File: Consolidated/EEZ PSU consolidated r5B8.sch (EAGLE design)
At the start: 517 parts, among them IC1 LTC3864, IC10 REF5025, IC11 DAC8552, IC12 ADG465SOT-23, IC13 TS5A9411DCKT, IC14 ADS1120, IC15 LP339D, IC16 LM25575, IC17 MC7812, IC18 TPD4E002DRLR, IC19 TPD2E001DZDR, IC2 MC79L05, IC20 ADUM3160BRWZ, IC21 TLC5925IDBQR, IC22 Si8641EC-B-IS1, IC23 SI8651EC-B-IS1, IC24 SI8651EC-B-IS1, IC25 LD1117ADT33TR, IC26 Si8641EC-B-IS1, IC27 PCA21125, IC28 AT25256B, IC29 W5500, IC3 MC78L05, IC30 BC857BS, IC31 TLC555, IC32 SN74LVC2G08DCTR, IC33 TPS3705-33D, IC34 SN74LV1T34DBVR, IC35 SN74LVC2G02DCTR, IC4 LM5574, IC5 LP2951SO8, IC6 TL072D, IC7 TL072D, IC8 OP27GSZ, IC9 MCP23S08-E/SO, J1 BS-244DSM-R, J2 BS-244DSM-G, J3 BS-244DSM-B, J4 BS-244DSM-R, J5 BS-244DSM-B, Q1 SUD19P06-60, Q10 MMBT5401, Q11 MMBT5401, Q12 MMBT5551, Q13 MMBT5551, Q14 BSS84P, Q15 2N7002, Q16 MMBT5551, Q17 MMBT5401, Q18 MMBT5551, Q19 MMBT5551, Q2 MMBT5401, Q20 BTA26-600, Q21 BTA26-600, Q22 IRLL014N, Q23 IRLML2246TRPBF, Q24 IRLML2246TRPBF, Q25 IRLML2246TRPBF, Q26 IRLML2246TRPBF, Q27 2N7002, Q28 IRLML2246TRPBF, Q29 2N7002, Q3 2N7002, Q30 2N7002, Q4 IRFP250N, Q5 BC857C, Q6 BC846C, Q7 BCP56-16.115, Q8 IRFR5410, Q9 BCP56-16.115, SW1 A101SYCQ04, SW2 1301.9316, X1 282836-3, X10 826629-5, X11 2411-01, X12 MC000006, X13 TSW-113-07-F-D, X14 MC000005, X15 TSW-113-07-F-D, X16 09185067324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

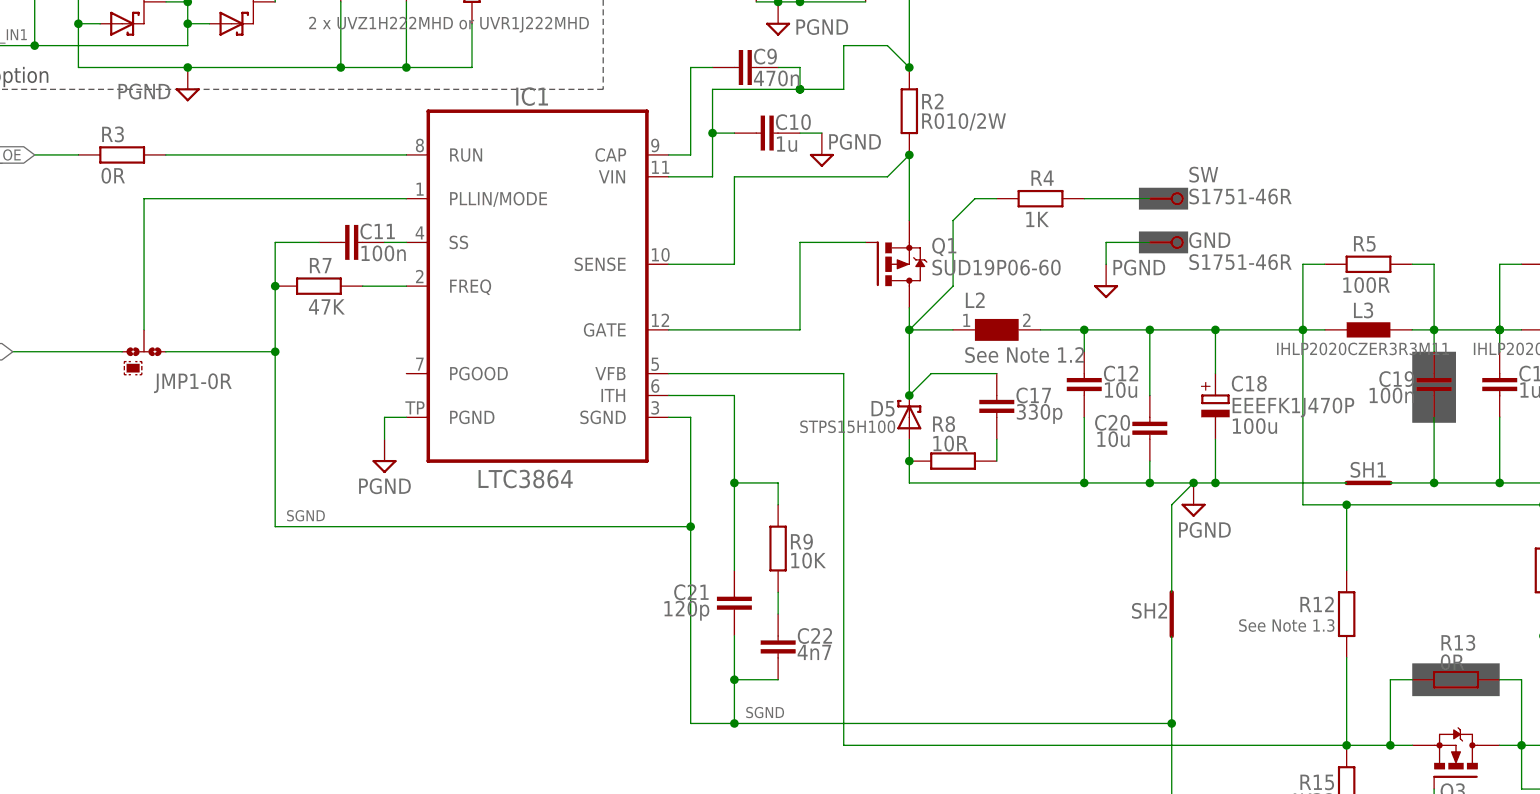
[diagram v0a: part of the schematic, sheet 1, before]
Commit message: Consolidated PCB, jumpers renumbering
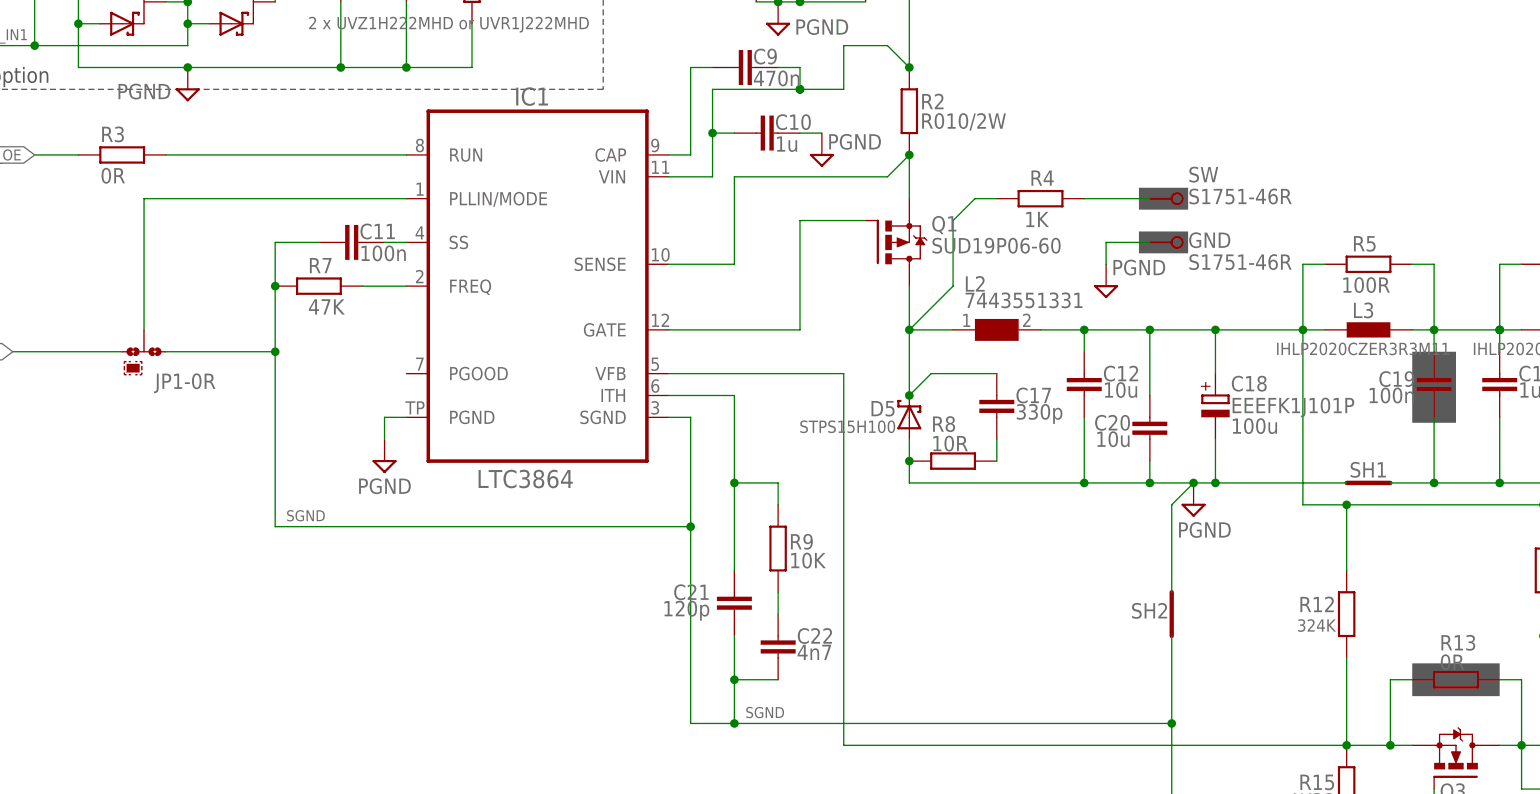
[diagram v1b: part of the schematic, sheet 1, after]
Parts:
- removed JMP1, JMP2: 0R-JUMPA, jump-0r-smd:0R-JUMPA
- added JP6, JP7: 0R-JUMPA, jump-0r-smd:0R-JUMPA
- C18: value EEEFK1J470P -> EEEFK1J101P
- D28: device diode:DIODE-DO214AC -> EEZ_Lib1:SCHOTTKYSOD123
- FB6, FB7: value 2506033007Y3 -> 60R@100MHz
- JP1: value 826926-2 -> 0R-JUMPA; device jumper:JP1E -> jump-0r-smd:0R-JUMPA
- JP3: value 0R-JUMPA -> 826926-2; device jump-0r-smd:0R-JUMPA -> jumper:JP1E
- L2: value See Note 1.2 -> 7443551331
- LED1: device led:LEDCHIPLED_0805 -> EEZ_Lib1:LED0805
- R12: value See Note 1.3 -> 324K
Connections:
- net !INT: now also JP2-0R.2; no longer JMP2-0R.2
- net !PS_DRDY: now also JP2-0R.3; no longer JMP2-0R.3
- net !PWD_RST: now also JP3.1; no longer JP1.1
- net +3V3: now also JP4-0R.3; no longer JP2-0R.3
- net +5V: now also JP4-0R.1; no longer JP2-0R.1
- net GND: now also JP3.2; no longer JP1.2
- net INT_EXP: now also JP2-0R.1; no longer JMP2-0R.1
- net MISO: now also JP7-0R.1; no longer JP5-0R.1
- net MODE: now also JP1-0R.2; no longer JMP1-0R.2
- net MOSI: now also JP6-0R.1; no longer JP4-0R.1
- net N$102: now also JP4-0R.2; no longer JP2-0R.2
- net N$104: now also JP7-0R.2; no longer JP5-0R.2
- net N$105: now also JP5-0R.2; no longer JP3-0R.2
- net N$106: now also JP6-0R.2; no longer JP4-0R.2
- net SCLK: now also JP5-0R.1; no longer JP3-0R.1
- net SGND: now also JP1-0R.1; no longer JMP1-0R.1
- net SYNC: now also JP1-0R.3; no longer JMP1-0R.3
- net TOUCH_DIN: now also JP6-0R.3; no longer JP4-0R.3
- net TOUCH_DOUT: now also JP7-0R.3; no longer JP5-0R.3
- net TOUCH_SCLK: now also JP5-0R.3; no longer JP3-0R.3
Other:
- note added: "Note 1.3: Use 240K for 30 VAC main transformer"
- note added: "See also Note 1.2"
- note added: "See also Note 1.3"
- note removed: "Note 1.3: Use 240K for 30 VAC or 324K for 40 VAC main transformer"
- moved on the sheet: JP4-0R, JP5-0R, Q1

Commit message: Fixed fan control, miniMELF replaced with SOD-323
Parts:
- added C157: 100n, rcl:C-EUC0603
- added D29: SKL16, EEZ_Lib1:SCHOTTKYSOD123
- C104: value 470n/100V -> 100n; device rcl:C-EUC1812 -> rcl:C-EUC0603
- C105, C110: value 10n -> 470n/100V; device rcl:C-EUC1206 -> rcl:C-EUC1812
- C106, C111: value UPW1J150MED -> 10n; device MyLib6:ECAPEEEFK+2.5MM -> rcl:C-EUC1206
- C107: value 10u -> UPW1J150MED; device rcl:C-EUC1206 -> MyLib6:ECAPEEEFK+2.5MM
- C108: value 10n -> 10u
- C109: value 470n/100V -> 10n; device rcl:C-EUC1812 -> rcl:C-EUC1206
- C112: value 10n -> UPW1J150MED; device rcl:C-EUC1206 -> MyLib6:ECAPEEEFK+2.5MM
- C113: value 100n -> 10n; device rcl:C-EUC0603 -> rcl:C-EUC1206
- C119: value 47u -> 100n; device MyLib6:ECAPPANASONIC_C -> rcl:C-EUC0603
- C120: value 10u -> 47u
- C121: value 100n -> 10u; device rcl:C-EUC0603 -> MyLib6:ECAPPANASONIC_C
- C125: value 10u -> 100n; device rcl:C-EUC1206 -> rcl:C-EUC0603
- C126: value 100n -> 10u; device rcl:C-EUC0603 -> rcl:C-EUC1206
- C127: value EECS5R5H105 -> 100n; device EEZ_Lib1:SUPER_CAP -> rcl:C-EUC0603
- C128: value 100n -> EECS5R5H105; device rcl:C-EUC0603 -> EEZ_Lib1:SUPER_CAP
- C130: value 22n -> 100n; device rcl:C-EUC0805 -> rcl:C-EUC0603
- C131: value 18p -> 22n
- C132: value 6n8 -> 18p; device rcl:C-EUC0603 -> rcl:C-EUC0805
- C133: value 10n -> 6n8; device rcl:C-EUC0805 -> rcl:C-EUC0603
- C134: value 6n8 -> 10n; device rcl:C-EUC0603 -> rcl:C-EUC0805
- C135: value 18p -> 6n8; device rcl:C-EUC0805 -> rcl:C-EUC0603
- C136: value 100n -> 18p; device rcl:C-EUC0603 -> rcl:C-EUC0805
- C144: value 10u -> 100n; device EEZ_Lib1:ECAP1206 -> rcl:C-EUC0603
- C145: value 4u7 -> 10u
- C146: value 10n -> 4u7; device rcl:C-EUC0805 -> EEZ_Lib1:ECAP1206
- C147, C156: value 100n -> 10n; device rcl:C-EUC0603 -> rcl:C-EUC0805
- C148, C152: value 47n -> 100n; device rcl:C-EUC0805 -> rcl:C-EUC0603
- C149, C153, C99: value 100n -> 47n; device rcl:C-EUC0603 -> rcl:C-EUC0805
- C154: value 10n -> 100n; device rcl:C-EUC0805 -> rcl:C-EUC0603
- C97: value 100u -> 10u; device EEZ_Lib1:ECAPPANASONIC_H -> MyLib6:ECAPPANASONIC_C
- C98: value 47n -> 100u; device rcl:C-EUC0805 -> EEZ_Lib1:ECAPPANASONIC_H
- D25: value SMBJ5.0A-TR -> BAS316; device MyLib6:DIODEDO214AA -> diode:DIODE-SOD323-W
- D26: value BAS316 -> SMBJ5.0A-TR; device diode:DIODE-SOD323-W -> MyLib6:DIODEDO214AA
- D27: value BAT54S -> BAS316; device diode:BAT54S -> diode:DIODE-SOD323-W
- D28: value SKL16 -> BAT54S; device EEZ_Lib1:SCHOTTKYSOD123 -> diode:BAT54S
- ZD4: value 13V -> BZX384-C15.115; device EEZ_Lib1:ZENER-DIODEMINIMELF -> EEZ_Lib1:ZENER-DIODESOD323
- ZD5: value 6V2 -> PDZ6.2B; device EEZ_Lib1:ZENER-DIODEMINIMELF -> EEZ_Lib1:ZENER-DIODESOD323
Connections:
- new net N$163: D21.C, X6-3.S
- net !MR: now also C153.2; no longer C152.2
- net +3V3: now also C108.1, C116.1, C118.1, C121.+, C123.1, C127.1, C131.1, C137.2, C144.1, C145.+, C150.2, C151.1, C152.2, C154.1, C157.1, D27.A; no longer C107.1, C114.1, C117.1, C120.+, C122.1, C126.1, C130.1, C136.2, C138.1, C144.+, C149.2, C150.1, C151.2, C153.1, C156.1, D26.A
- net +5V: now also C100.1, C120.+, C126.2, D26.C; no longer C119.+, C125.2, C99.1, D25.C
- net 12VDC: now also C98.+
- net 1V2O: now also C147.2; no longer C146.2
- net AC_IN1: now also X2-1.1; no longer X2-2.1
- net AC_IN2: now also X2-2.1; no longer X2-1.1
- net AUX_FAN_SENSE: now also D21.A; no longer X6-3.S
- net CH1_GND: now also C114.2, C117.2, C148.2, C149.1; no longer C113.2, C116.2, C147.2, C148.1
- net CH1_VDD: now also C114.1, C117.1, C148.1; no longer C113.1, C116.1, C147.1
- net CH2_GND: now also C119.2, C122.2; no longer C118.2, C121.2
- net CH2_VDD: now also C119.1, C122.1; no longer C118.1, C121.1
- net DC+: now also L1-1.1; no longer L1-2.1
- net DC-: now also L1-2.1, X1-3.1; no longer L1-1.1, X1-1.1
- net DC_OUT: now also L1-1.2; no longer L1-2.2
- net EARTH: now also C106.2, C109.1, C111.2, C113.1, C131.2, C134.2, X1-1.1; no longer C105.2, C108.1, C110.2, C112.1, C130.2, C133.2, X1-3.1
- net ENC_A: now also C155.2, MCU-ADCH.ADC8; no longer C154.2, MCU-ADCH.ADC14
- net ENC_B: now also C156.1, MCU-ADCH.ADC9; no longer C155.1, MCU-ADCH.ADC15
- net ETH_IN+: now also C135.1; no longer C134.1
- net ETH_IN-: now also C133.1; no longer C132.1
- net FAN_OUT: now also C99.2; no longer C98.2
- net GND: now also C100.2, C103.2, C108.2, C116.2, C118.2, C121.-, C123.2, C126.1, C127.2, C128.-, C130.1, C132.2, C136.2, C138.1, C144.2, C145.-, C147.1, C150.1, C151.2, C153.1, C154.2, C155.1, C157.2, C97.-, D26.A, D28.A1, L1-2.2; no longer C102.2, C107.2, C114.2, C117.2, C119.-, C122.2, C123.1, C126.2, C127.-, C128.1, C131.2, C135.2, C136.1, C138.2, C144.-, C146.1, C149.1, C150.2, C151.1, C153.2, C154.1, C155.2, C99.2, D21.A, D27.A1, L1-1.2
- net GNDA: now also C146.-; no longer C145.-
- net N$107: now also C128.+; no longer C127.+
- net N$109: now also C124.2, D27.C; no longer C123.2, D26.C
- net N$111: now also C132.1; no longer C131.1
- net N$112: now also C136.1; no longer C135.1
- net N$113: now also C133.2; no longer C132.2
- net N$115: now also C135.2; no longer C134.2
- net N$124: now also C134.1; no longer C133.1
- net N$132: now also C138.2; no longer C137.2
- net N$136: now also C149.2; no longer C148.2
- net N$139: now also D28.C1A2; no longer D27.C1A2
- net N$144: now also D28.C2; no longer D27.C2
- net N$148: now also D29.C; no longer D28.C
- net N$149: now also D29.A; no longer D28.A
- net N$155: now also D23.C; no longer D22.C
- net N$156: now also D24.C; no longer D23.C
- net N$84: now also C99.1; no longer C98.1
- net N$86: now also C98.-; no longer C97.-
- net N$87: now also C104.1; no longer C103.1
- net N$90: now also C101.1; no longer C100.1
- net N$91: now also C103.1; no longer C102.1
- net N$92: now also D22.C; no longer D21.C
- net N$93: now also D25.C; no longer D24.C
- net N$94: now also C105.2; no longer C104.2
- net N$95: now also C110.2; no longer C109.2
- net NTC1: now also C125.2; no longer C124.2
- net NTC2: now also C130.2; no longer C129.2
- net OUT1+: now also C106.1; no longer C105.1
- net OUT1-: now also C107.-, C109.2; no longer C106.-, C108.2
- net OUT2+: now also C111.1, C112.+; no longer C109.1, C111.+
- net OUT2-: now also C113.2; no longer C112.2
- net PWR_IN1+: now also C105.1, C107.+; no longer C104.1, C106.+
- net PWR_IN2-: now also C112.-; no longer C111.-
- net TEMP_ANALOG: now also C129.2; no longer C128.2
- net TOCAP: now also C146.+; no longer C145.+
- net XUSB_GND: now also C101.2, C102.1, C104.2; no longer C100.2, C101.1, C103.2
- net XUSB_VBUS: now also C102.2; no longer C101.2
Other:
- moved on the sheet: C100, C101, C102, C103, C105, C108, C109, C110, C114, C115, C116, C117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
